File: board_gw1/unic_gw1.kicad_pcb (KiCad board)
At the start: 4 copper layers, 50 x 15.2 mm, 127 parts, among them Q1 2N7002, Q10 2N7002, Q11 2N7002, Q12 2N7002, Q13 2N7002, Q14 2N7002, Q15 2N7002, Q16 2N7002, Q17 2N7002, Q18 2N7002, Q19 2N7002, Q2 2N7002, Q20 2N7002, Q21 2N7002, Q22 2N7002, Q23 2N7002, Q24 2N7002, Q25 2N7002, Q26 2N7002, Q27 2N7002, Q28 2N7002, Q29 2N7002, Q3 2N7002, Q30 2N7002, Q31 2N7002, Q32 2N7002, Q33 2N7002, Q34 2N7002, Q35 2N7002, Q36 2N7002, Q37 2N7002, Q38 2N7002, Q39 2N7002, Q4 2N7002, Q40 2N7002, Q41 2N7002, Q5 2N7002, Q6 2N7002, Q7 2N7002, Q8 2N7002, Q9 2N7002, U1 GW1N-LV9QN88C6_I5_, U3 MIC5203-3.3BM5, U4 APS6404L-3SQR-ZR, U5 MIC5504-1.2YM5, U6 AP62150Z6, U7 W25Q16JVUXIQ, X1 27MHz

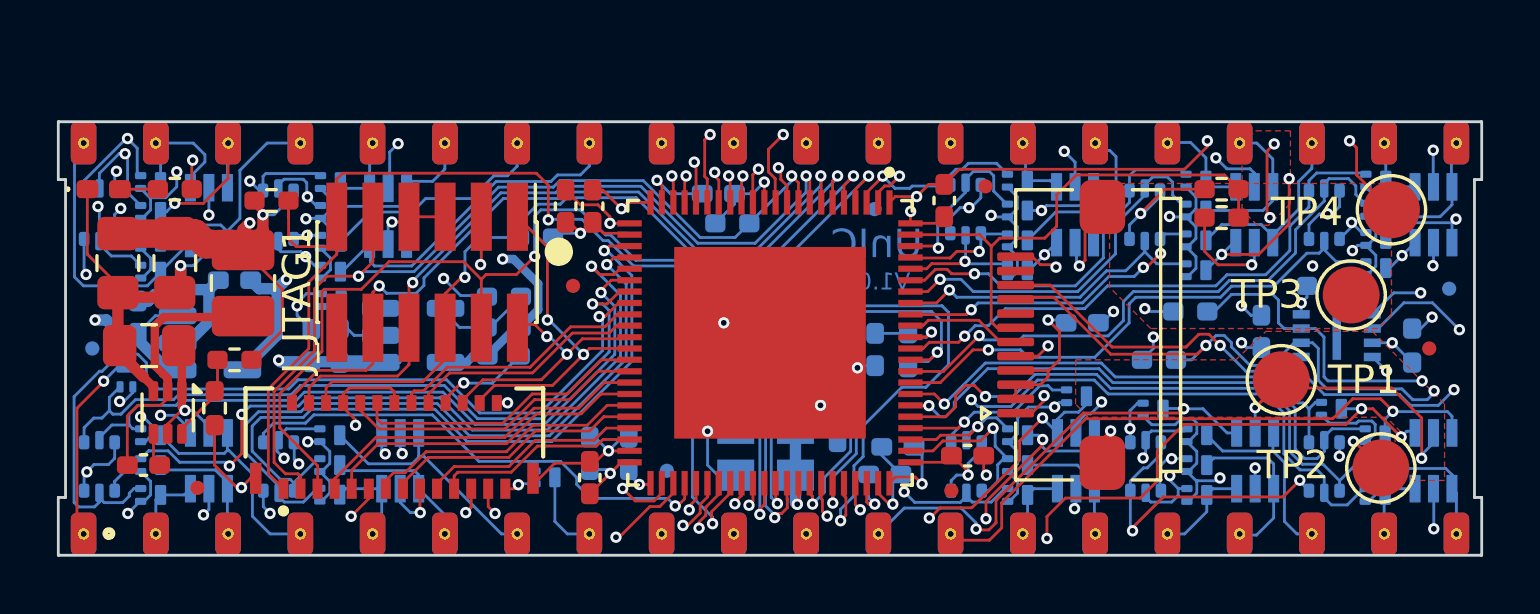
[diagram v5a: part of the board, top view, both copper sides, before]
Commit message: Lots of (local) footprint cleanup and readying for board release.
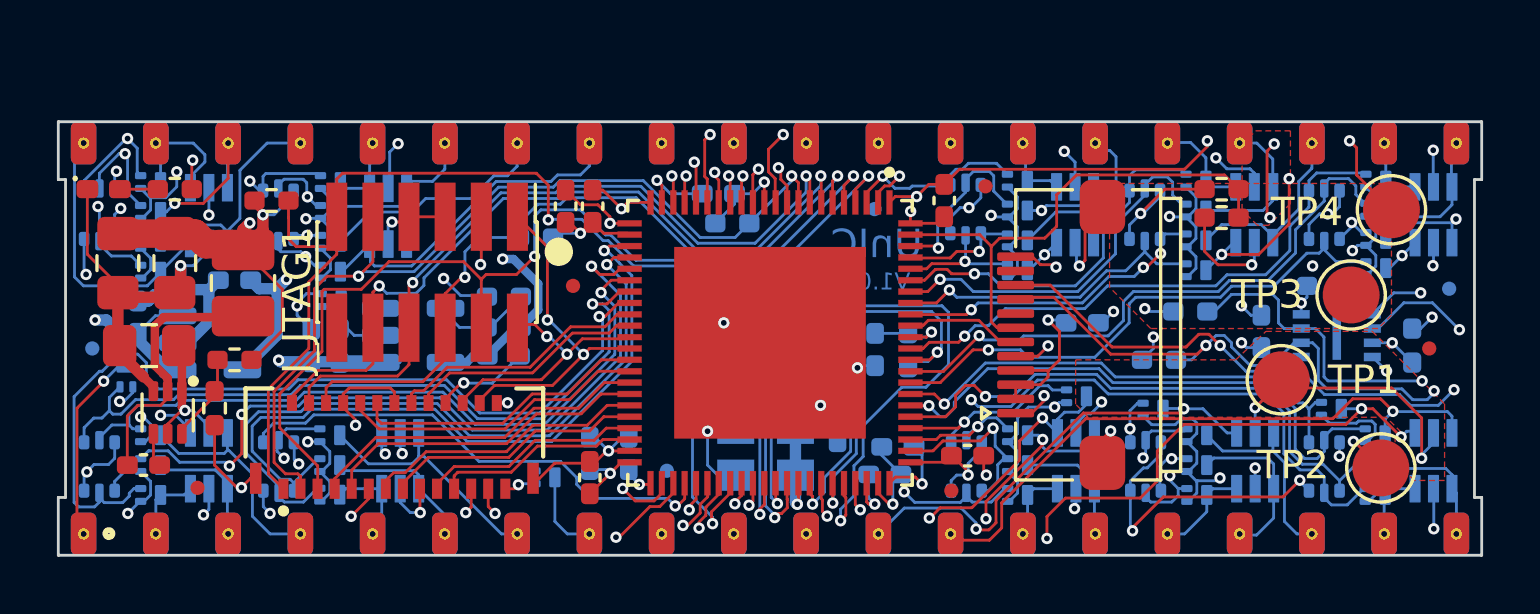
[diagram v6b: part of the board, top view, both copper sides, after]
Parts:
- C1, C10, C11, C13, C14, C15, C16, C17, C18, C19, C2, C20, C21, C22, C23, C3, C4, C6, C9: footprint Capacitor_SMD:C_0402_1005Metric_Pad0.74x0.62mm_HandSolder -> UNIC:C_0402_1005Metric_Pad0.74x0.62mm_HandSolder
- C5, C7, C8: footprint Capacitor_SMD:C_0805_2012Metric_Pad1.18x1.45mm_HandSolder -> UNIC:C_0805_2012Metric_Pad1.18x1.45mm_HandSolder
- D21, D22, D23, D24, D25, D26, D27, D28, D29, D30: footprint Package_TO_SOT_SMD:SOT-666 -> UNIC:SOT-666
- FID1, FID2, FID3, FID4, FID5, FID6, FID7, FID8, FID9: footprint Fiducial:Fiducial_0.5mm_Mask1mm -> UNIC:Fiducial_0.5mm_Mask1mm
- L1: footprint Inductor_SMD:L_1008_2520Metric_Pad1.43x2.20mm_HandSolder -> UNIC:L_1008_2520Metric_Pad1.43x2.20mm_HandSolder
- LED_DONE1: footprint LED_SMD:LED_0402_1005Metric_Pad0.77x0.64mm_HandSolder -> UNIC:LED_0402_1005Metric_Pad0.77x0.64mm_HandSolder
- R1, R10, R11, R12, R13, R14, R15, R16, R17, R2, R3, R4, R5, R6, R7, R8, R9: footprint Resistor_SMD:R_0402_1005Metric_Pad0.72x0.64mm_HandSolder -> UNIC:R_0402_1005Metric_Pad0.72x0.64mm_HandSolder
- TP1, TP2, TP3, TP4: footprint TestPoint:TestPoint_Pad_D2.0mm -> UNIC:TestPoint_Pad_D2.0mm
- U3, U5: footprint Package_TO_SOT_SMD:SOT-23-5 -> UNIC:SOT-23-5
- U6: footprint Package_TO_SOT_SMD:SOT-563 -> UNIC:SOT-563
